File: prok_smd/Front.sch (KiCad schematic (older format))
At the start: 29 parts, among them CON1 microSD_Card, J12 Conn_01x05_Male, J17 Conn_01x05_Male, J5 TIME_CV, J6 CHANNEL_CV, J7 RESET_CV, J8 OUT, SW1 SW_Push_LED, X1 50k, Y1 50k

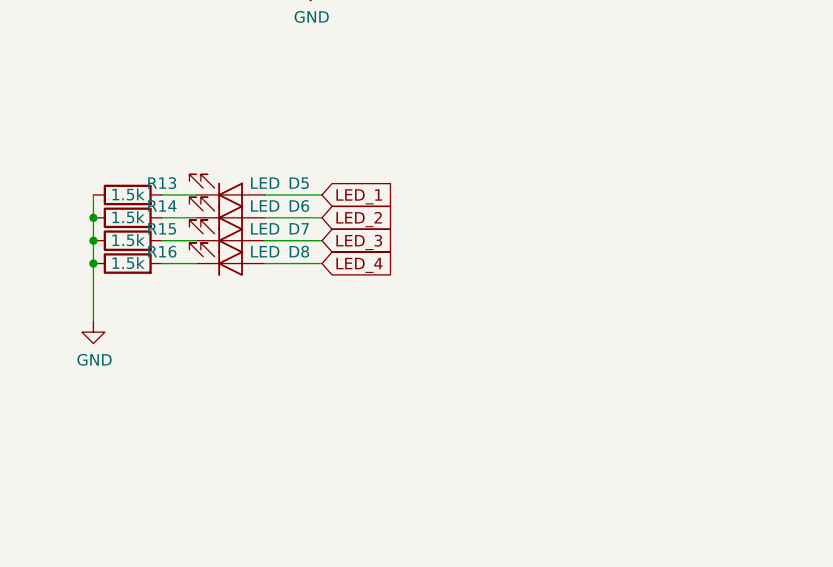
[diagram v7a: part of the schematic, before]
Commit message: :construction: Add some caps to smoothe PWM
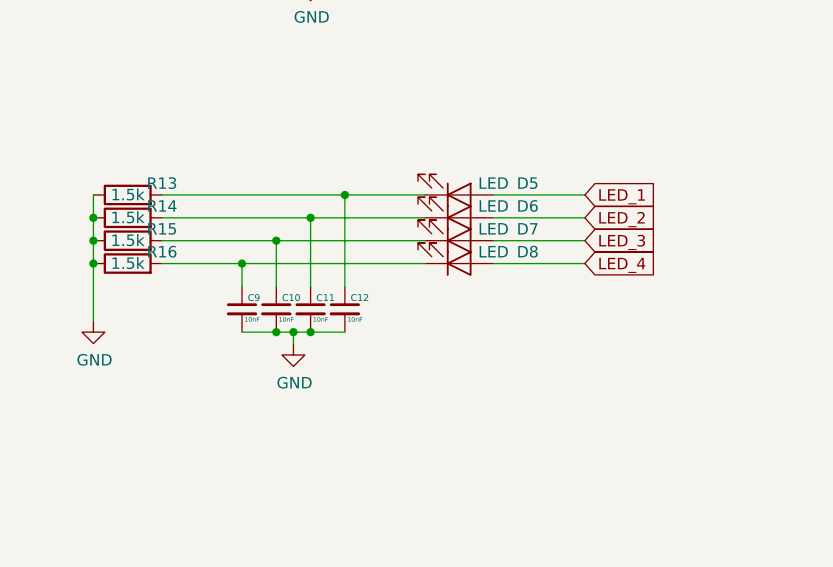
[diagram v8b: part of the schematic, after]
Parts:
- added C10, C11, C12, C9: 10nF, Capacitor_SMD:C_0603_1608Metric, symbol Device:C_Small
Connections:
- net GND: now also C10.2, C11.2, C12.2, C9.2
- net at D5.1 (K), R13.2: now also C12.1
- net at D6.1 (K), R14.2: now also C11.1
- net at D7.1 (K), R15.2: now also C10.1
- net at D8.1 (K), R16.2: now also C9.1
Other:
- moved on the sheet: D5, D6, D7, D8
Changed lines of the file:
@@
 L Device:LED D5
 U 1 1 5D284BD7
-P 7500 4100
-F 0 "D5" H 7800 4050 50  0000 C CNN
-F 1 "LED" H 7650 4050 50  0000 C CNN
-F 2 "4ms-footprints:LED-3MM-SQUARE-ANODE" H 7500 4100 50  0001 C CNN
-F 3 "~" H 7500 4100 50  0001 C CNN
-	1    7500 4100
+P 8500 4100
+F 0 "D5" H 8800 4050 50  0000 C CNN
+F 1 "LED" H 8650 4050 50  0000 C CNN
+F 2 "4ms-footprints:LED-3MM-SQUARE-ANODE" H 8500 4100 50  0001 C CNN
+F 3 "~" H 8500 4100 50  0001 C CNN
+	1    8500 4100
 	1    0    0    1
 $EndComp
@@
 L Device:LED D6
 U 1 1 5D284ED2
-P 7500 4200
-F 0 "D6" H 7800 4150 50  0000 C CNN
-F 1 "LED" H 7650 4150 50  0000 C CNN
-F 2 "4ms-footprints:LED-3MM-SQUARE-ANODE" H 7500 4200 50  0001 C CNN
-F 3 "~" H 7500 4200 50  0001 C CNN
-	1    7500 4200
+P 8500 4200
+F 0 "D6" H 8800 4150 50  0000 C CNN
+F 1 "LED" H 8650 4150 50  0000 C CNN
+F 2 "4ms-footprints:LED-3MM-SQUARE-ANODE" H 8500 4200 50  0001 C CNN
+F 3 "~" H 8500 4200 50  0001 C CNN
+	1    8500 4200
 	1    0    0    1
 $EndComp
@@
 L Device:LED D7
 U 1 1 5D284F12
-P 7500 4300
-F 0 "D7" H 7800 4250 50  0000 C CNN
-F 1 "LED" H 7650 4250 50  0000 C CNN
-F 2 "4ms-footprints:LED-3MM-SQUARE-ANODE" H 7500 4300 50  0001 C CNN
-F 3 "~" H 7500 4300 50  0001 C CNN
-	1    7500 4300
+P 8500 4300
+F 0 "D7" H 8800 4250 50  0000 C CNN
+F 1 "LED" H 8650 4250 50  0000 C CNN
+F 2 "4ms-footprints:LED-3MM-SQUARE-ANODE" H 8500 4300 50  0001 C CNN
+F 3 "~" H 8500 4300 50  0001 C CNN
+	1    8500 4300
 	1    0    0    1
 $EndComp
@@
 L Device:LED D8
 U 1 1 5D284F54
-P 7500 4400
-F 0 "D8" H 7800 4350 50  0000 C CNN
-F 1 "LED" H 7650 4350 50  0000 C CNN
-F 2 "4ms-footprints:LED-3MM-SQUARE-ANODE" H 7500 4400 50  0001 C CNN
-F 3 "~" H 7500 4400 50  0001 C CNN
-	1    7500 4400
+P 8500 4400
+F 0 "D8" H 8800 4350 50  0000 C CNN
+F 1 "LED" H 8650 4350 50  0000 C CNN
+F 2 "4ms-footprints:LED-3MM-SQUARE-ANODE" H 8500 4400 50  0001 C CNN
+F 3 "~" H 8500 4400 50  0001 C CNN
+	1    8500 4400
 	1    0    0    1
 $EndComp
-Wire Wire Line
-	7200 4400 7350 4400
-Wire Wire Line
-	7350 4300 7200 4300
-Wire Wire Line
-	7200 4200 7350 4200
-Wire Wire Line
-	7350 4100 7200 4100
 Wire Wire Line
 	6900 4100 6900 4200
@@
 	1    0    0    -1
 $EndComp
-Text GLabel 7900 4100 2    50   Input ~ 0
+Text GLabel 9050 4100 2    50   Input ~ 0
 LED_1
-Text GLabel 7900 4200 2    50   Input ~ 0
+Text GLabel 9050 4200 2    50   Input ~ 0
 LED_2
-Text GLabel 7900 4300 2    50   Input ~ 0
+Text GLabel 9050 4300 2    50   Input ~ 0
 LED_3
-Text GLabel 7900 4400 2    50   Input ~ 0
+Text GLabel 9050 4400 2    50   Input ~ 0
 LED_4
-Wire Wire Line
-	7650 4400 7900 4400
-Wire Wire Line
-	7900 4300 7650 4300
-Wire Wire Line
-	7650 4200 7900 4200
-Wire Wire Line
-	7900 4100 7650 4100
 $Comp
 L 4ms-mech:microSD_Card CON1
@@
 NoConn ~ 2750 6950
 NoConn ~ 2750 7150
+$Comp
+L Device:C_Small C12
+U 1 1 5EF4EF51
+P 8000 4600
+F 0 "C12" H 8025 4650 30  0000 L CNN
+F 1 "10nF" H 8010 4555 20  0000 L CNN
+F 2 "Capacitor_SMD:C_0603_1608Metric" H 8000 4600 50  0001 C CNN
+F 3 "~" H 8000 4600 50  0001 C CNN
+	1    8000 4600
+	1    0    0    -1
+$EndComp
+Wire Wire Line
+	8000 4500 8000 4100
+Wire Wire Line
+	7850 4500 7850 4200
+$Comp
+L power:GND #PWR0119
+U 1 1 5EF5E363
+P 7775 4750
+F 0 "#PWR0119" H 7775 4500 50  0001 C CNN
+F 1 "GND" H 7780 4577 50  0000 C CNN
+F 2 "" H 7775 4750 50  0001 C CNN
+F 3 "" H 7775 4750 50  0001 C CNN
+	1    7775 4750
+	1    0    0    -1
+$EndComp
+Wire Wire Line
+	7775 4700 7775 4750
+Connection ~ 7775 4700
+Wire Wire Line
+	7550 4700 7700 4700
+Wire Wire Line
+	7775 4700 7850 4700
+$Comp
+L Device:C_Small C11
+U 1 1 5EF62D0C
+P 7850 4600
+F 0 "C11" H 7875 4650 30  0000 L CNN
+F 1 "10nF" H 7860 4555 20  0000 L CNN
+F 2 "Capacitor_SMD:C_0603_1608Metric" H 7850 4600 50  0001 C CNN
+F 3 "~" H 7850 4600 50  0001 C CNN
+	1    7850 4600
+	1    0    0    -1
+$EndComp
+Connection ~ 7850 4700
+Wire Wire Line
+	7850 4700 8000 4700
+$Comp
+L Device:C_Small C10
+U 1 1 5EF631E0
+P 7700 4600
+F 0 "C10" H 7725 4650 30  0000 L CNN
+F 1 "10nF" H 7710 4555 20  0000 L CNN
+F 2 "Capacitor_SMD:C_0603_1608Metric" H 7700 4600 50  0001 C CNN
+F 3 "~" H 7700 4600 50  0001 C CNN
+	1    7700 4600
+	1    0    0    -1
+$EndComp
+Connection ~ 7700 4700
+Wire Wire Line
+	7700 4700 7775 4700
+$Comp
+L Device:C_Small C9
+U 1 1 5EF63501
+P 7550 4600
+F 0 "C9" H 7575 4650 30  0000 L CNN
+F 1 "10nF" H 7560 4555 20  0000 L CNN
+F 2 "Capacitor_SMD:C_0603_1608Metric" H 7550 4600 50  0001 C CNN
+F 3 "~" H 7550 4600 50  0001 C CNN
+	1    7550 4600
+	1    0    0    -1
+$EndComp
+Wire Wire Line
+	7200 4300 7700 4300
+Wire Wire Line
+	7200 4100 8000 4100
+Wire Wire Line
+	8650 4100 9050 4100
+Wire Wire Line
+	9050 4200 8650 4200
+Wire Wire Line
+	8650 4300 9050 4300
+Wire Wire Line
+	9050 4400 8650 4400
+Connection ~ 7850 4200
+Connection ~ 8000 4100
+Wire Wire Line
+	8000 4100 8350 4100
+Wire Wire Line
+	7850 4200 8350 4200
+Wire Wire Line
+	7200 4400 7550 4400
+Wire Wire Line
+	7200 4200 7850 4200
+Wire Wire Line
+	7700 4500 7700 4300
+Connection ~ 7700 4300
+Wire Wire Line
+	7700 4300 8350 4300
+Wire Wire Line
+	7550 4500 7550 4400
+Connection ~ 7550 4400
+Wire Wire Line
+	7550 4400 8350 4400
 $EndSCHEMATC
